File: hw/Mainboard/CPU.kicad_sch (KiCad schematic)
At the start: 12 parts, among them SW1 RESET, SW4 NMI, U11 W65C02S, U12 AS6C1008

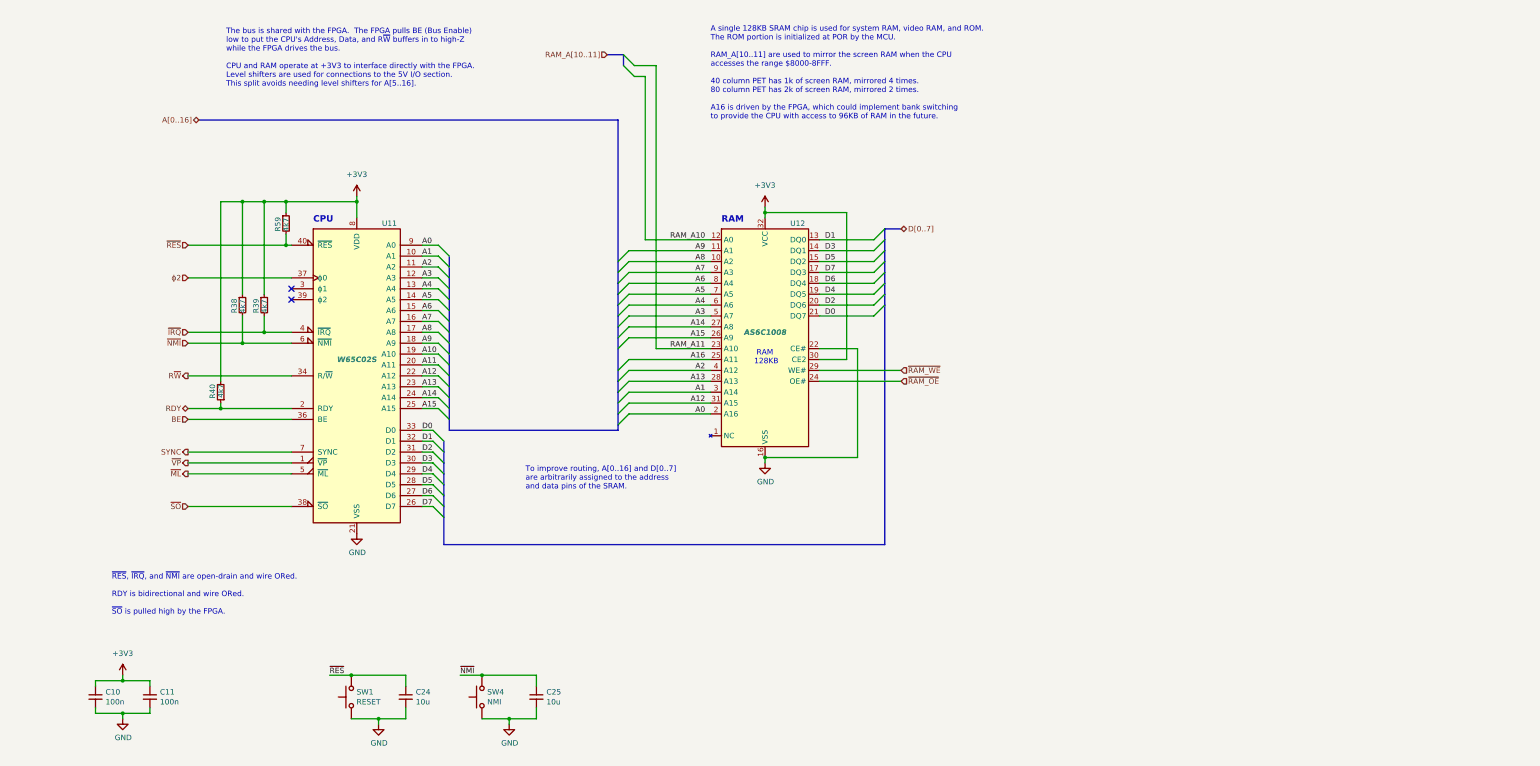
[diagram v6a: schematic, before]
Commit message: hw: replace ram_ce with ram_a15
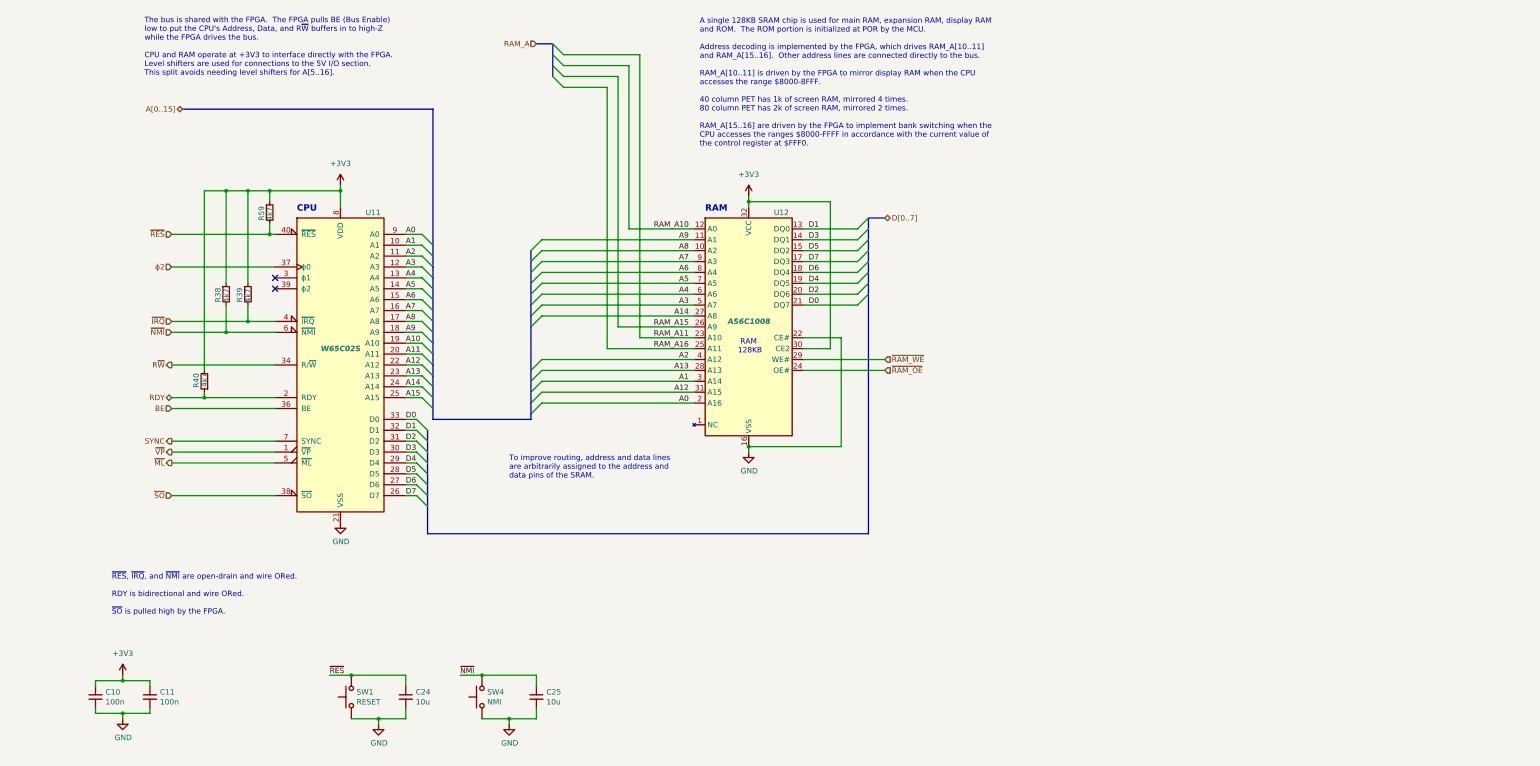
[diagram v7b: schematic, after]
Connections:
- net A15: no longer U12.26 (A9)
- net A16 renamed RAM_A16
- new net RAM_A15: U12.26 (A9)
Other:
- note added: "A single 128KB SRAM chip is used for main RAM, expansion RAM, display RAM and ROM. The ROM portion is initialized at POR by the MCU. Address decoding is implemented by the FPGA, which drives RAM_A[10..11] and RAM_A[15..16]. Other address lines are connected directly to the bus. RAM_A[10..11] is driven by the FPGA to mirror display RAM when the CPU accesses the range $8000-8FFF. 40 column PET has 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"
- note added: "To improve routing, address and data lines are arbitrarily assigned to the address and data pins of the SRAM."
- note removed: "A single 128KB SRAM chip is used for system RAM, video RAM, and ROM. The ROM portion is initialized at POR by the MCU. RAM_A[10..11] are used to mirror the screen RAM when the CPU accesses the range $8000-8FFF. 40 column PET has 1k of screen RAM, mirrored 4 times. 80 column PET has 2k of screen RAM, mirrored 2 times. A16 is driven by the FPGA, which could implement bank switching to provide the C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"
- note removed: "To improve routing, A[0..16] and D[0..7] are arbitrarily assigned to the address and data pins of the SRAM."
- moved on the sheet: R38, R39, R40, R59, U11, U12

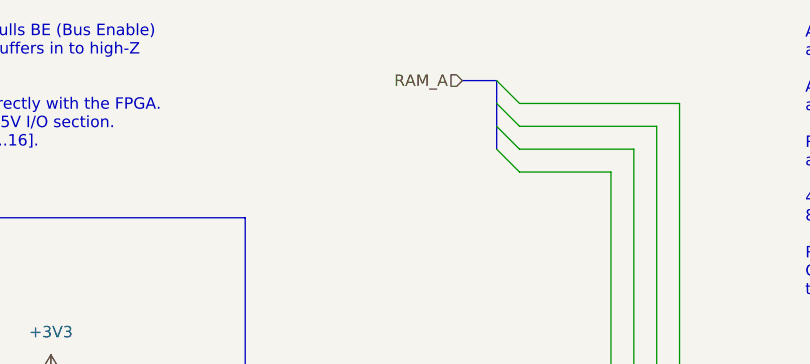
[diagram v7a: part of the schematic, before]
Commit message: hw: move DVI to separate hierarchical sheet, fix buses, annotate power
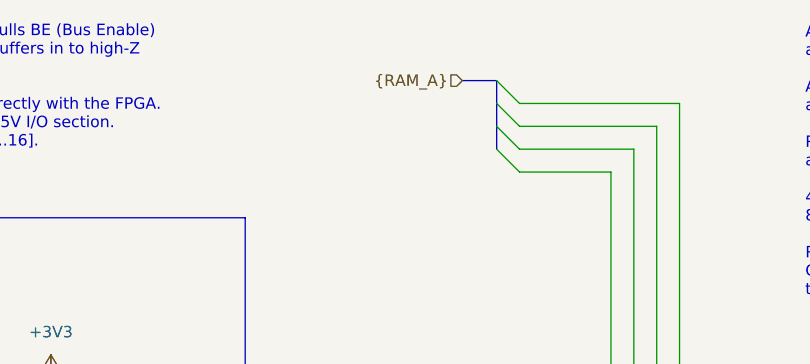
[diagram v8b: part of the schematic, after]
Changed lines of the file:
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@@
     (effects (font (size 1.27 1.27)) (justify right))
   )
-  (hierarchical_label "RAM_A" (shape input) (at 138.43 31.75 180)
+  (hierarchical_label "{RAM_A}" (shape input) (at 138.43 31.75 180)
     (effects (font (size 1.27 1.27)) (justify right))
   )
@@
   (symbol (lib_id "power:+3V3") (at 41.91 179.07 0) (unit 1)
     (in_bom yes) (on_board yes) (fields_autoplaced)
-    (property "Reference" "#PWR?" (id 0) (at 41.91 182.88 0)
-      (effects (font (size 1.27 1.27)) hide)
-    )
+    (property "Reference" "#PWR07" (id 0) (at 41.91 182.88 0)
+      (effects (font (size 1.27 1.27)) hide)
+    )
